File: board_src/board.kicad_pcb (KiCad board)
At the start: 2 copper layers, 220 x 150 mm, 148 parts, among them IC1 PCF8563TS_4,118, IC2 M24C02-WMN6TP, IC3 DS18B20+, IC4 FT232RNL-TUBE, IC5 MCP3202-CI_MS, IC6 MCP4921-E_P, J1 Conn_01x05, J10 Conn_01x02_Pin, J11 Conn_01x03, J12 112J-TDAR-R01, J13 Conn_01x03, J14 Conn_01x07, J15 Conn_01x03, J16 Conn_01x05, J17 Conn_01x05, J18 Conn_02x20_Counter_Clockwise, J19 Conn_02x07_Odd_Even, J2 Conn_01x05, J20 Conn_02x20_Counter_Clockwise, J21 Conn_02x20_Counter_Clockwise, J22 Conn_02x20_Counter_Clockwise, J23 Conn_01x04, J24 Conn_01x08, J25 Conn_01x04, J26 Conn_01x20_Socket, J27 Conn_01x20_Socket, J28 Conn_01x04, J29 Conn_01x08, J3 Conn_01x06, J30 Conn_01x05, J31 Conn_01x05, J32 Conn_02x05_Odd_Even, J34 USB_C_Receptacle_USB2.0_16P, J36 Conn_01x20_Socket, J37 Conn_01x20_Socket, J4 Conn_01x04, J40 Conn_01x01_Pin, J41 Conn_01x01_Pin, J42 Conn_01x01_Pin, J43 Conn_01x01_Pin, J44 Conn_01x01_Pin, J46 Conn_01x01_Pin, J5 Conn_01x08, J6 Conn_01x02_Pin, J7 Conn_01x16_Socket, J8 Conn_01x04, J9 Conn_01x02_Pin, Q1 NPN, Q2 SS8550, Q3 SS8550, Q4 SS8550, Q5 SS8550, Q7 BC107, U1 Pico, U4 Pico, Y2 Crystal

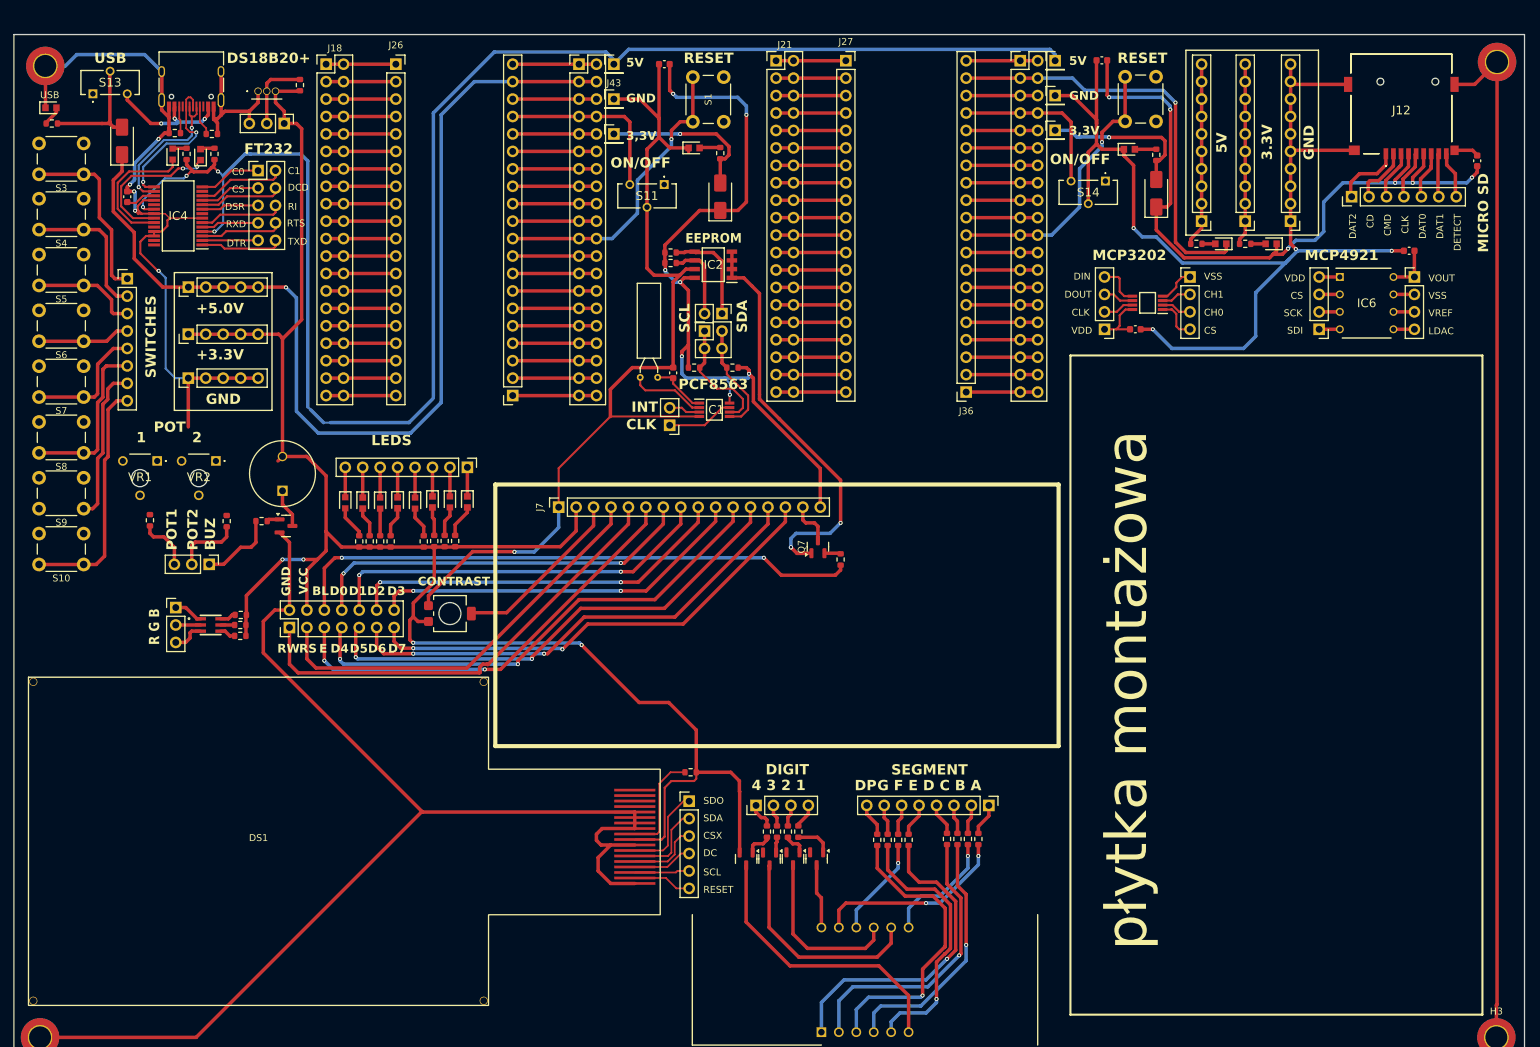
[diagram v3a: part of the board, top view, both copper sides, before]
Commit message: poprawione polaczenia diod i wartosci opornikow, aktualizacja niektorych elementow ze wzgledu na braki w magazynie
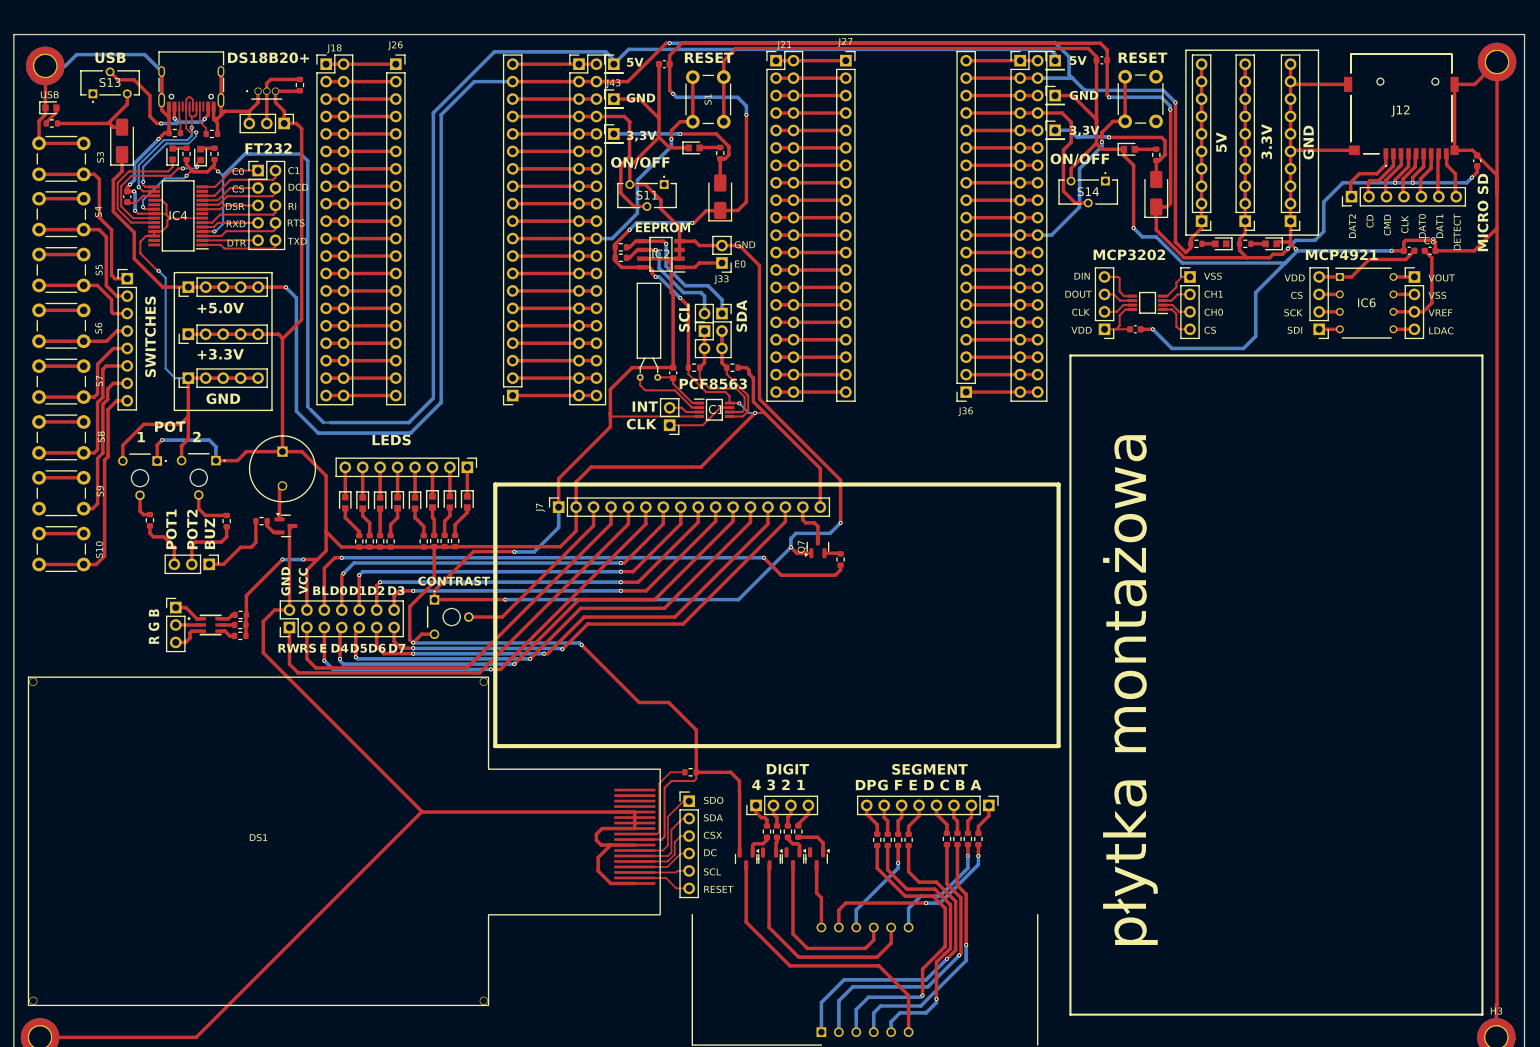
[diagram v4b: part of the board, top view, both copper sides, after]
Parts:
- added C8: 100n, Capacitor_SMD:C_0603_1608Metric, F.Cu at (206.2, 31.5)
- added J33: Conn_01x02_Pin, Connector_PinHeader_2.54mm:PinHeader_1x02_P2.54mm_Vertical, F.Cu at (103.1, 33.3)
- R11, R12, R37, R38, R39, R40, R41, R42: value 221 -> 220
- R19: value 10k -> 4.7k
- R21, R22, R23: value 68 -> 220
- RV1: footprint Potentiometer_SMD:Potentiometer_Bourns_3314R-GM5_Vertical -> footprints:PT6KV251A2020
- S11, S13, S14: footprint footprints:CLSB12C01 -> footprints:JS102011CQN
- moved IC2 7.77 mm to (94.2, 32.0)
- moved R15 7.28 mm to (88.4, 32.5)
- moved R16 7.28 mm to (88.4, 31.0)
- moved LS1 5.70 mm to (39.1, 60.7), turned to 180 degrees
- moved RV1 3.00 mm to (61.3, 82.3), turned to -90 degrees
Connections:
- C7 pad 1: Net-(IC6-VOUT) -> Net-(IC6-VDD)
- IC2 pad 1: GND -> Net-(IC2-E0)
- J30 pad 1: Net-(J30-Pin_1) -> +3.3V
- J30 pad 10: Net-(J30-Pin_1) -> +3.3V
- J30 pad 2: Net-(J30-Pin_1) -> +3.3V
- J30 pad 3: Net-(J30-Pin_1) -> +3.3V
- J30 pad 4: Net-(J30-Pin_1) -> +3.3V
- J30 pad 5: Net-(J30-Pin_1) -> +3.3V
- J30 pad 6: Net-(J30-Pin_1) -> +3.3V
- J30 pad 7: Net-(J30-Pin_1) -> +3.3V
- J30 pad 8: Net-(J30-Pin_1) -> +3.3V
- J30 pad 9: Net-(J30-Pin_1) -> +3.3V
- J31 pad 1: Net-(J31-Pin_1) -> VSYS
- J31 pad 10: Net-(J31-Pin_1) -> VSYS
- J31 pad 2: Net-(J31-Pin_1) -> VSYS
- J31 pad 3: Net-(J31-Pin_1) -> VSYS
- J31 pad 4: Net-(J31-Pin_1) -> VSYS
- J31 pad 5: Net-(J31-Pin_1) -> VSYS
- J31 pad 6: Net-(J31-Pin_1) -> VSYS
- J31 pad 7: Net-(J31-Pin_1) -> VSYS
- J31 pad 8: Net-(J31-Pin_1) -> VSYS
- J31 pad 9: Net-(J31-Pin_1) -> VSYS
- LED16 pad 1: +3.3V -> GND
- LED17 pad 1: VSYS -> GND
- LS1 pad 1: Net-(LS1-+) -> +3.3V
- LS1 pad 2: +3.3V -> Net-(LS1--)
- Q1 pad 1: Net-(Q1-B) -> Net-(LS1--)
- Q1 pad 2: GND -> Net-(Q1-B)
- Q1 pad 3: Net-(LS1-+) -> GND
- R8 pad 1: Net-(J30-Pin_1) -> +3.3V
- R9 pad 1: Net-(J31-Pin_1) -> VSYS
- S1 pad 2: unconnected-(S1-Pad2) -> GND
- S10 pad 2: unconnected-(S10-Pad2) -> GND
- S12 pad 2: unconnected-(S12-Pad2) -> GND
- S3 pad 2: unconnected-(S3-Pad2) -> GND
- S4 pad 2: unconnected-(S4-Pad2) -> GND
- S5 pad 2: unconnected-(S5-Pad2) -> GND
- S6 pad 2: unconnected-(S6-Pad2) -> GND
- S7 pad 2: unconnected-(S7-Pad2) -> GND
- S8 pad 2: unconnected-(S8-Pad2)_1 -> GND
- S9 pad 2: unconnected-(S9-Pad2) -> GND
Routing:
- net GND: track 830.0 -> 1072.4 mm
- net +3.3V: track 485.9 -> 644.1 mm, vias 17 -> 19
- net VSYS: track 210.6 -> 307.3 mm, vias 2 -> 3
- net Net-(J31-Pin_1): track 26.8 -> 0.00 mm
- net Net-(J30-Pin_1): track 26.5 -> 0.00 mm
- net Net-(IC6-VDD): track 3.02 -> 15.5 mm
- net Net-(IC6-VREF): track 3.05 -> 14.2 mm
- net Net-(IC2-SDA): track 15.1 -> 21.9 mm, vias 0 -> 1
- net Net-(IC2-SCL): track 11.8 -> 18.6 mm, vias 0 -> 1
- net Net-(R14-Pad2): track 0.00 -> 6.49 mm
- net Net-(IC2-E0): track 0.00 -> 6.44 mm
- net /b4: track 25.7 -> 32.2 mm
- net Net-(LS1-+): track 6.33 -> 0.00 mm
- net /d4: track 24.2 -> 30.4 mm
- net Net-(S13-B): track 18.1 -> 23.2 mm
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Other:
- board text added: "E0"

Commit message: dodany tranzystor BS123
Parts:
- removed U1, U4: Pico, footprints:RPi_Pico_SMD_TH
- added Q6: BSS123, Package_TO_SOT_SMD:SOT-23, F.Cu at (86.3, 100.7)
- added R17: 10, Resistor_SMD:R_0603_1608Metric, F.Cu at (91.6, 99.2)
- IC3: footprint footprints:DS18B20 -> Package_TO_SOT_THT:TO-92L_Inline_Wide
- IC5: footprint footprints:SOP65P490X110-8N -> Package_SO:SOIC-8_5.3x5.3mm_P1.27mm
- J3: footprint Connector_PinHeader_2.54mm:PinHeader_1x06_P2.54mm_Vertical -> Connector_PinHeader_2.54mm:PinHeader_1x07_P2.54mm_Vertical
- R1: value 100 -> 4.7
- R6, R7, R8, R9: value 249 -> 220
- moved DS4 33.9 mm to (250.4, 78.9)
- moved R1 9.35 mm to (91.6, 101.2), turned to 0 degrees
- moved J15 5.56 mm to (28.4, 80.8), turned to -90 degrees
- moved J23 3.47 mm to (174.8, 35.3)
- moved C4 3.30 mm to (166.4, 44.2)
- moved LED1 3.22 mm to (25.9, 87.7), turned to 0 degrees
- moved IC3 2.69 mm to (34.3, 7.37)
- moved J3 2.32 mm to (98.6, 109.3)
- moved R21 1.97 mm to (31.9, 86.2)
- moved R22 1.94 mm to (31.9, 87.6)
- moved R23 1.94 mm to (31.9, 89.2)
- moved IC5 1.27 mm to (166.4, 39.1)
- moved J4 0.85 mm to (158.0, 42.9)
- moved J37 0.76 mm to (73.4, 52.6)
- moved LED14 0.55 mm to (99.3, 17.0)
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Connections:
- DS1 pad 10: Net-(DS1-LED-A) -> +3.3V
- DS1 pad 11: GND -> /Wyświetlacz/KATODA
- DS1 pad 12: GND -> /Wyświetlacz/KATODA
- DS1 pad 13: GND -> /Wyświetlacz/KATODA
- DS1 pad 14: GND -> /Wyświetlacz/KATODA
- J3 pad 1: Net-(DS1-SDO) -> /Wyświetlacz/R0
- J3 pad 2: Net-(DS1-SDA) -> Net-(DS1-SDO)
- J3 pad 3: Net-(DS1-~{CSX}) -> Net-(DS1-SDA)
- J3 pad 4: Net-(DS1-D/C) -> Net-(DS1-~{CSX})
- J3 pad 5: Net-(DS1-SCL) -> Net-(DS1-D/C)
- J3 pad 6: Net-(DS1-~{RESET}) -> Net-(DS1-SCL)
- R1 pad 1: +3.3V -> /Wyświetlacz/R0
- R1 pad 2: Net-(DS1-LED-A) -> GND
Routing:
- net GND: track 1072.4 -> 1239.1 mm, vias 13 -> 19
- net +3.3V: track 644.1 -> 702.3 mm, vias 19 -> 25
- net /Wyświetlacz/KATODA: track 0.00 -> 23.2 mm
- net /Wyświetlacz/R0: track 0.00 -> 15.6 mm, vias 0 -> 1
- net Net-(DS1-LED-A): track 15.2 -> 0.00 mm
- net Net-(LED1-A_RED): track 2.30 -> 10.6 mm
- net Net-(LED1-A_GREEN): track 2.02 -> 8.95 mm
- net Net-(J5-Pin_7): track 22.8 -> 28.4 mm
- net Net-(LED1-A_BLUE): track 2.31 -> 6.29 mm
- net Net-(Q6-S): track 0.00 -> 3.71 mm
- net /Wyświetlacz segmentowy/c: track 36.8 -> 40.1 mm
- net Net-(IC5-VDD/VREF): track 8.17 -> 10.9 mm
- net /Wyświetlacz segmentowy/d: track 41.9 -> 44.3 mm
- net Net-(IC3-DQ): track 10.9 -> 12.9 mm
- net Net-(J15-Pin_3): track 4.28 -> 6.11 mm
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- added copper zone on B.Cu, net GND
- added copper zone on F.Cu, net GND
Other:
- board text added: "3V3"
- board text added: "3V3_EN"
- board text added: "ADC_VREF"
- board text added: "AGND"
- board text added: "GP0"
- board text added: "GP1"
- board text added: "GP10"
- board text added: "GP11"
- board text added: "GP12"
- board text added: "GP13"
- board text added: "GP14"
- board text added: "GP15"
- board text added: "GP16"
- board text added: "GP17"
- board text added: "GP18"
- board text added: "GP19"
- board text added: "GP2"
- board text added: "GP20"
- board text added: "GP21"
- board text added: "GP22"
- board text added: "GP26"
- board text added: "GP27"
- board text added: "GP28"
- board text added: "GP3"
- board text added: "GP4"
- board text added: "GP5"
- board text added: "GP6"
- board text added: "GP7"
- board text added: "GP8"
- board text added: "GP9"
- board text added: "R0"
- board text added: "RUN"
- board text added: "SWCLK"
- board text added: "SWDIO"
- board text added: "VBUS"
- board text added: "VSYS"

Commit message: najnowsza wersja
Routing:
- net /d4: track 30.4 -> 31.0 mm
- net GND: track 1239.1 -> 1238.5 mm

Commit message: finalna wersja, naniesione poprawki
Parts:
- removed DS4: RC1602B-BIW-ESX, footprints:RC1602BBIWESX
- IC5: value MCP3202-CI_MS -> MCP3202
- R1: value 4.7 -> 4.7k
- R13, R24, R25, R26, R27, R28, R29, R30: value 221 -> 220
- R4: value R -> 4.7k
- moved J23 18.2 mm to (158.2, 42.9), turned to 180 degrees
- moved J4 18.2 mm to (174.5, 35.3), turned to 0 degrees
- moved C4 10.1 mm to (169.2, 34.5), turned to 180 degrees
- moved Q6 0.54 mm to (85.9, 100.3)
- turned IC5 to 0 degrees
- renumbered S3 to S1, S4 to S2, S5 to S3, S6 to S4, S7 to S5, S8 to S6, S9 to S7, S10 to S8
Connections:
- Q6 pad 2: Net-(Q6-S) -> GND
- Q6 pad 3: GND -> Net-(Q6-D)
- R17 pad 1: Net-(Q6-S) -> Net-(Q6-D)
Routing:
- net GND: track 1238.5 -> 1227.3 mm, vias 19 -> 21
- net Net-(Q6-D): track 0.00 -> 6.20 mm
- net Net-(Q6-S): track 3.71 -> 0.00 mm
- net +3.3V: track 702.5 -> 699.5 mm
- net Net-(IC5-VDD/VREF): track 10.9 -> 8.00 mm
- net /d4: track 31.0 -> 32.0 mm
- net (no net): vias 0 -> 24
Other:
- board text added: "Autor projektu: Aleksandra Gierad Promotor: dr inż. Dariusz Tefelski 2025r."
- board text added: "LCD"
- board text added: "USB POWER"
- board text removed: "R0"
